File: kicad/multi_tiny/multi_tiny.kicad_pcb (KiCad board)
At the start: 2 copper layers, 105 x 91 mm, 59 parts, among them J1 Conn_02x03_Odd_Even, J2 28pin ZIF, J8 Conn_01x25, SW1 SW_SPDT, SW2 SW_SPDT, SW3 SW_SPDT, SW4 SW_SPST, U1 CD4052B, U2 CD4052B, U3 CD4052B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

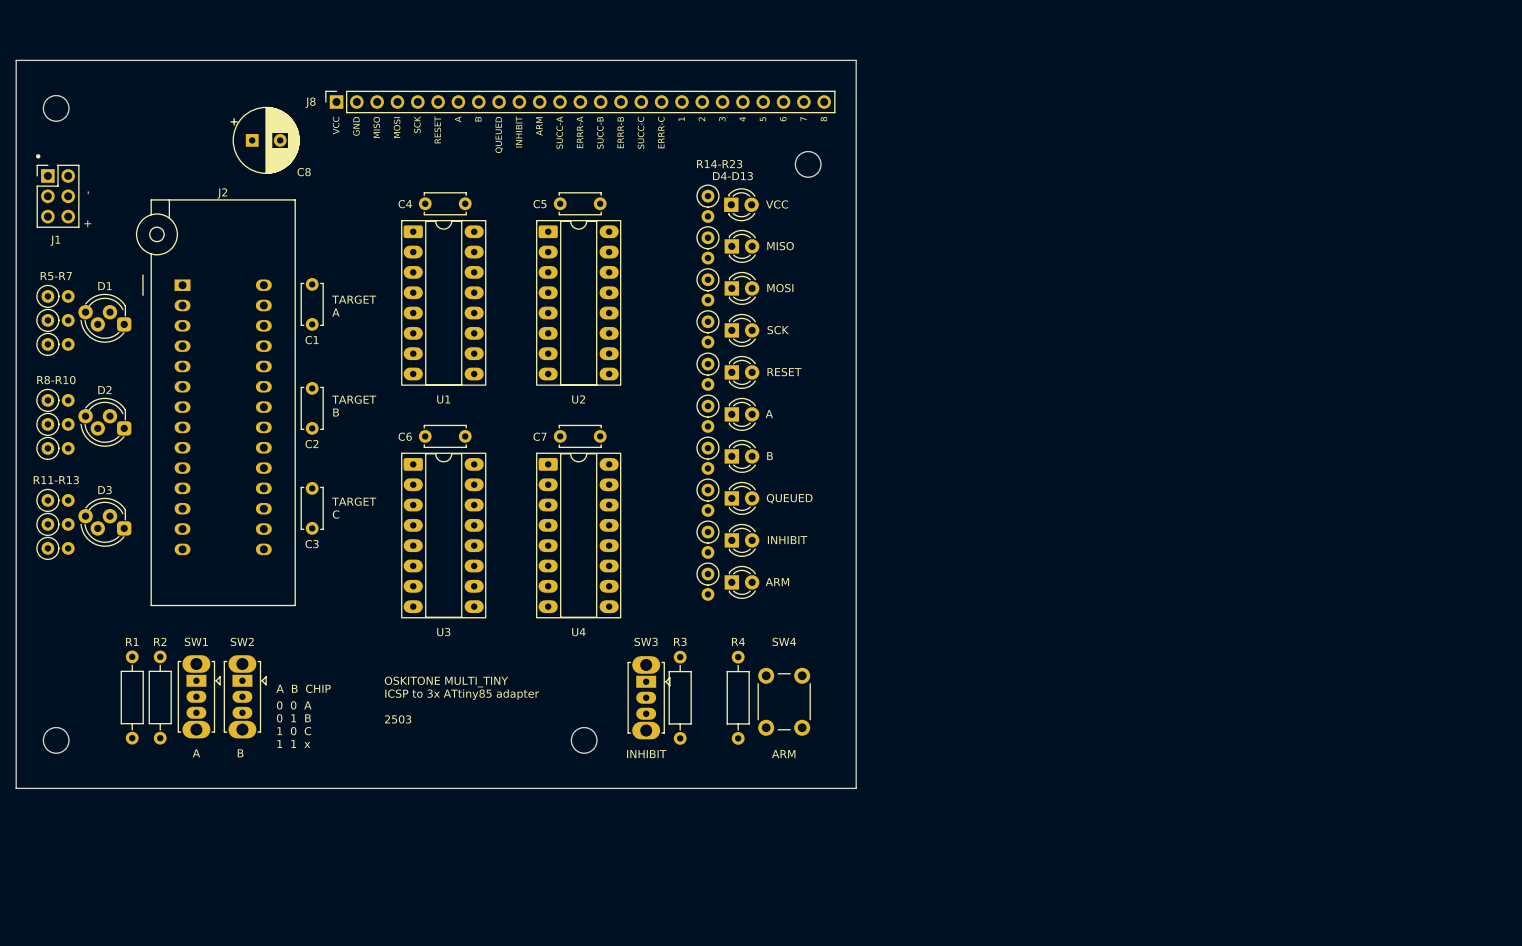
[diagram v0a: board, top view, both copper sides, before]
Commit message: Re-layout for flanked ZIF
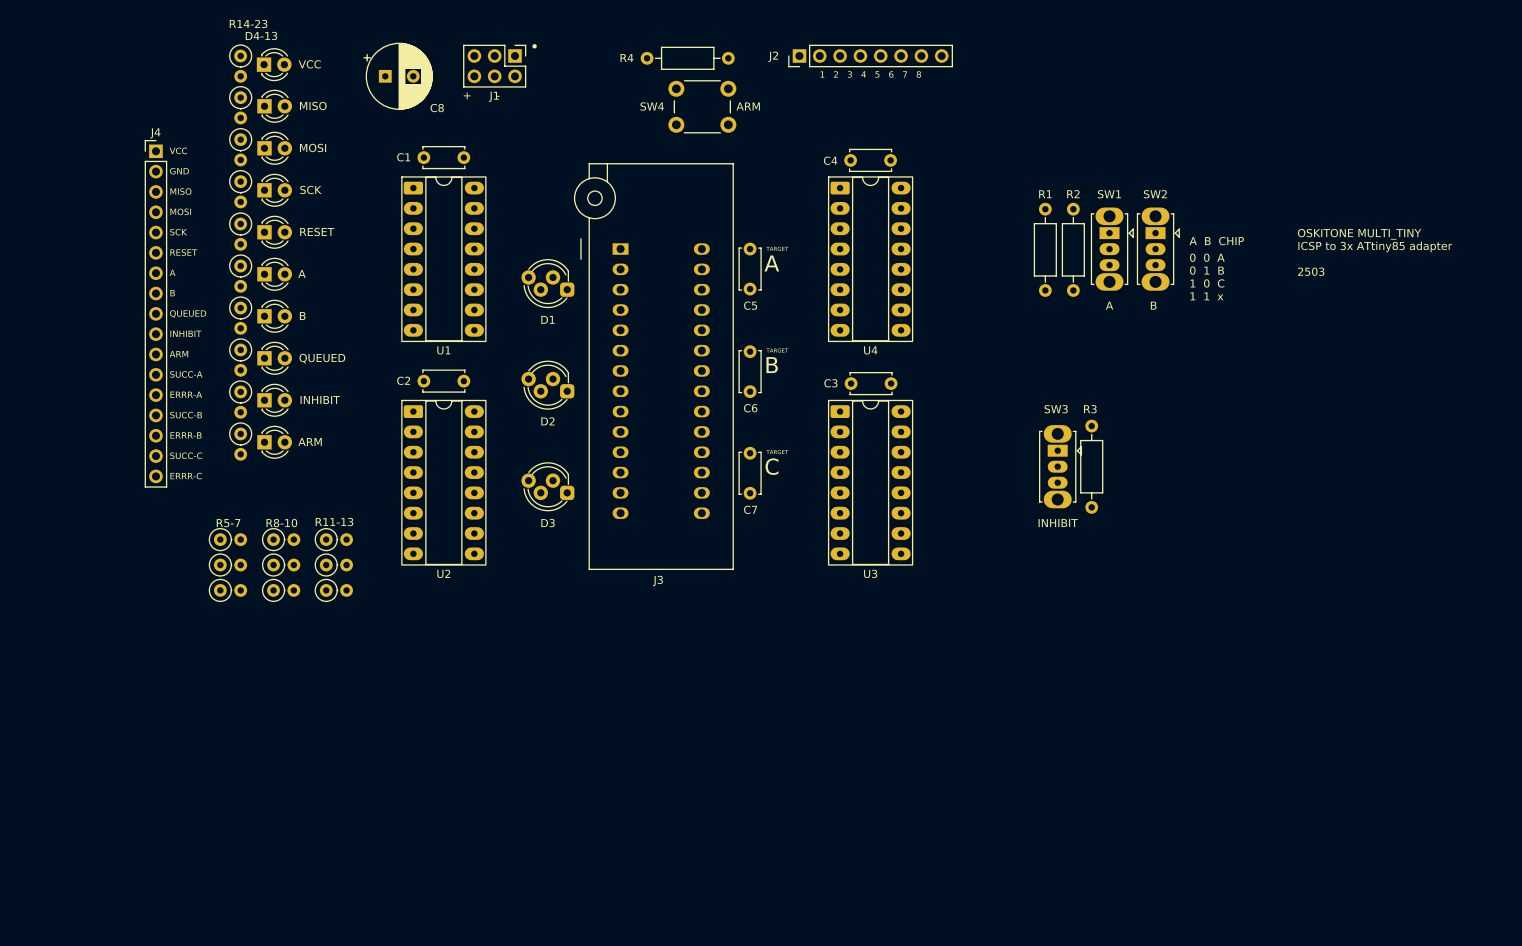
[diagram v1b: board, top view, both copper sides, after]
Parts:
- removed J8: Conn_01x25, Connector_PinSocket_2.54mm:PinSocket_1x25_P2.54mm_Vertical
- removed REF** (x4): MountingHole_3.2mm_M3, MountingHole:MountingHole_3.2mm_M3
- added J2: Conn_01x08, Connector_PinHeader_2.54mm:PinHeader_1x08_P2.54mm_Vertical, F.Cu at (168.9, 44.5)
- added J4: Conn_01x17, Connector_PinHeader_2.54mm:PinHeader_1x17_P2.54mm_Vertical, F.Cu at (88.5, 56.4)
- moved R1 127.1 mm to (199.6, 63.6)
- moved R2 127.1 mm to (203.1, 63.6)
- moved SW1 127.1 mm to (207.7, 66.6)
- moved SW2 127.1 mm to (213.4, 66.6)
- moved R4 75.7 mm to (149.9, 44.7), turned to 0 degrees
- moved SW4 75.0 mm to (153.5, 48.5), turned to 0 degrees
- moved C3 68.6 mm to (175.4, 85.4), turned to 0 degrees
- moved R14 61.0 mm to (99.1, 44.5)
- moved R15 61.0 mm to (99.1, 49.7)
- moved R16 61.0 mm to (99.1, 54.9)
- moved R17 61.0 mm to (99.1, 60.2)
- moved R18 61.0 mm to (99.1, 65.5)
- moved R19 61.0 mm to (99.1, 70.7)
- moved R20 61.0 mm to (99.1, 76.0)
- moved R21 61.0 mm to (99.1, 81.2)
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- renumbered J2 to J3
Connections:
- U3 pad 1: 4-A -> 3-A
- U3 pad 12: 3-A -> 4-A
- U3 pad 13: 3 -> 4
- U3 pad 14: 3-B -> 4-B
- U3 pad 15: 3-C -> 4-C
- U3 pad 2: 4-C -> 3-C
- U3 pad 3: 4 -> 3
- U3 pad 5: 4-B -> 3-B
- U4 pad 1: 8-A -> 7-A
- U4 pad 12: 7-A -> 8-A
- U4 pad 13: 7 -> 8
- U4 pad 14: 7-B -> 8-B
- U4 pad 15: 7-C -> 8-C
- U4 pad 2: 8-C -> 7-C
- U4 pad 3: 8 -> 7
- U4 pad 5: 8-B -> 7-B
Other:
- board outline removed
- board text added: "1 2 3 4 5 6 7 8"
- board text added: "C"
- board text added: "D4-13"
- board text added: "R11-13"
- board text added: "R14-23"
- board text added: "R5-7"
- board text added: "R8-10"
- board text added: "TARGET"
- board text added: "TODO: - test ZIF socket on print - mounting holes - rig holes on ZIF X rows - fix ICSP label? - header breadboard accessible"
- board text added: "VCC GND MISO MOSI SCK RESET A B QUEUED INHIBIT ARM SUCC-A ERRR-A SUCC-B ERRR-B SUCC-C ERRR-C"
- board text removed: "D4-D13"
- board text removed: "R11-R13"
- board text removed: "R14-R23"
- board text removed: "R5-R7"
- board text removed: "R8-R10"
- board text removed: "TARGET A"
- board text removed: "TARGET B"
- board text removed: "TARGET C"
- board text removed: "VCC GND MISO MOSI SCK RESET A B QUEUED INHIBIT ARM SUCC-A ERRR-A SUCC-B ERRR-B SUCC-C ERRR-C 1 2 3 4 5 6 7 8"

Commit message: Re-layout
* Fix ZIF dimensions
* IO refinements: ditch inhibit switch, pullups
  on external controls, add clear button
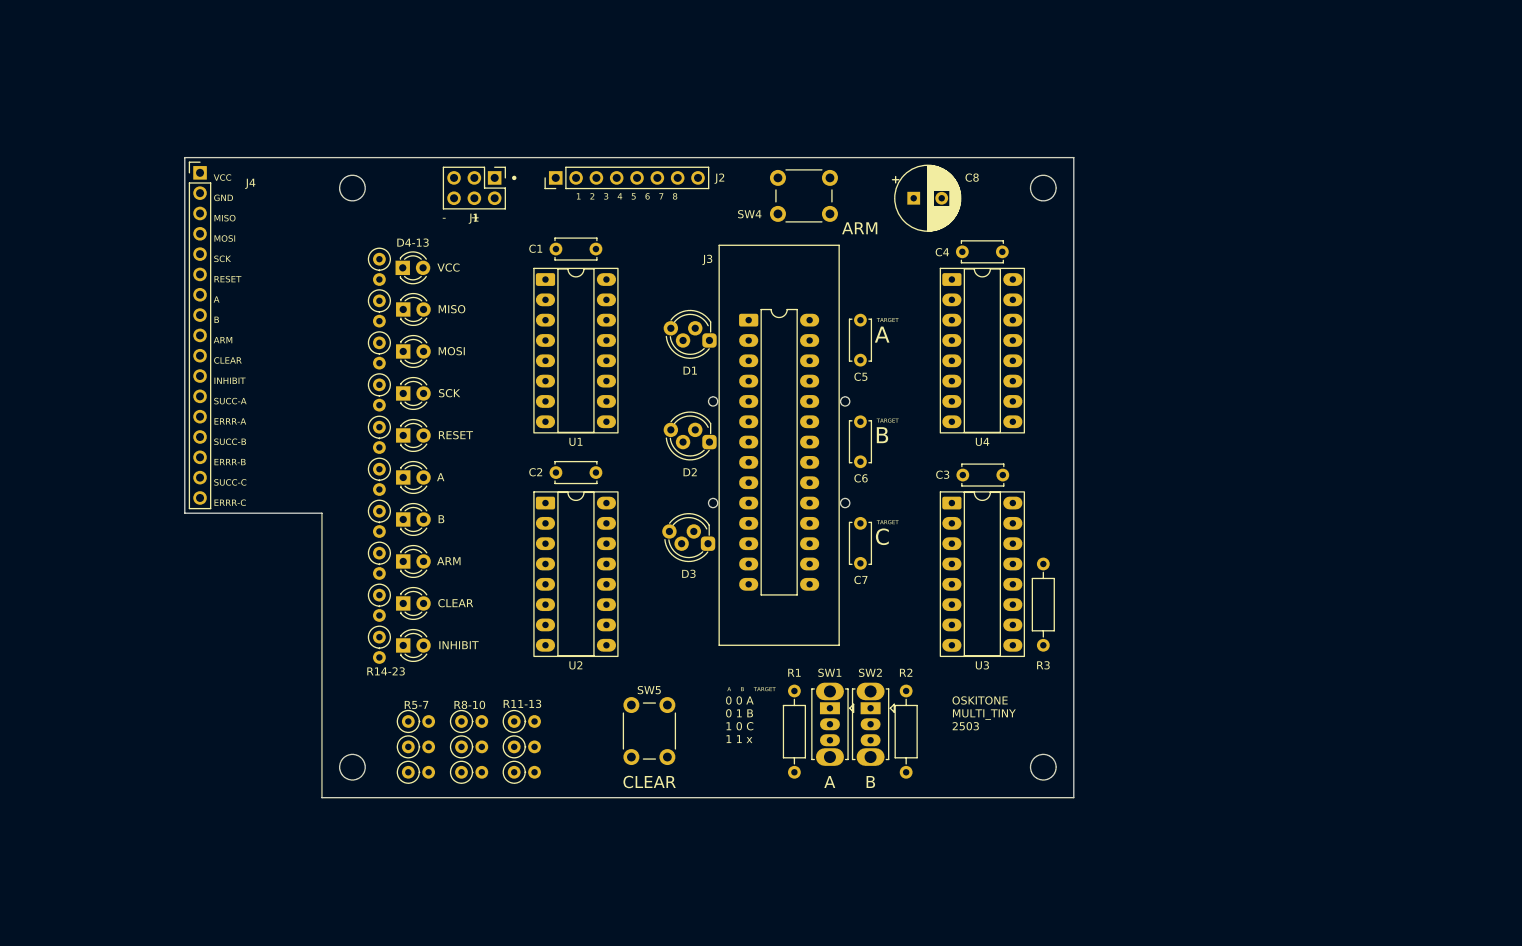
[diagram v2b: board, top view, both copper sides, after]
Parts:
- removed R4: 10k, Resistor_THT:R_Axial_DIN0207_L6.3mm_D2.5mm_P10.16mm_Horizontal
- removed SW3: SW_SPDT, Button_Switch_THT:SW_Slide_SPDT_Straight_CK_OS102011MS2Q
- added ?: , , F.Cu at (174.6, 100.3)
- added REF**: MountingHole_3.2mm_M3, MountingHole:MountingHole_3.2mm_M3, F.Cu at (113.0, 61.0)
- added REF**: ToolingHole_1.152mm, MountingHole:ToolingHole_1.152mm, F.Cu at (174.6, 87.6)
- added REF**: ToolingHole_1.152mm, MountingHole:ToolingHole_1.152mm, F.Cu at (158.1, 100.3)
- added REF**: MountingHole_3.2mm_M3, MountingHole:MountingHole_3.2mm_M3, F.Cu at (199.4, 61.0)
- added REF**: ToolingHole_1.152mm, MountingHole:ToolingHole_1.152mm, F.Cu at (158.1, 87.6)
- added REF**: MountingHole_3.2mm_M3, MountingHole:MountingHole_3.2mm_M3, F.Cu at (199.4, 133.3)
- added REF**: MountingHole_3.2mm_M3, MountingHole:MountingHole_3.2mm_M3, F.Cu at (113.0, 133.3)
- added SW5: SW_SPST, Button_Switch_THT:SW_PUSH_6mm, F.Cu at (147.9, 132.1)
- D11: value QUEUED -> ARM
- D12: value INHIBIT -> CLEAR
- D13: value ARM -> INHIBIT
- J3: footprint Socket:DIP_Socket-28_W6.9_W7.62_W10.16_W12.7_W13.5_3M_228-4817-00-0602J -> Package_DIP:DIP-28_W7.62mm_LongPads
- moved SW2 69.3 mm to (177.8, 126.0)
- moved SW1 68.9 mm to (172.7, 126.0)
- moved R1 67.9 mm to (168.3, 123.8)
- moved C8 67.8 mm to (183.2, 62.2)
- moved R2 63.7 mm to (182.2, 123.8)
- moved J2 34.1 mm to (138.4, 59.7)
- moved R13 32.7 mm to (133.3, 134.0)
- moved R7 32.7 mm to (120.0, 134.0)
- moved R10 32.7 mm to (126.7, 134.0)
- moved R11 32.7 mm to (133.3, 127.6)
- moved R12 32.7 mm to (133.3, 130.8)
- moved R5 32.7 mm to (120.0, 127.6)
- moved R6 32.7 mm to (120.0, 130.8)
- moved R8 32.7 mm to (126.7, 127.6)
- moved R9 32.7 mm to (126.7, 130.8)
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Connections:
- J4 pad 10: INHIBIT -> CLEAR
- J4 pad 11: ARM -> INHIBIT
- J4 pad 9: QUEUED -> ARM
- R21 pad 1: QUEUED -> ARM
- R22 pad 1: INHIBIT -> CLEAR
- R23 pad 1: ARM -> INHIBIT
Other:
- board outline added: 111.1 x 80 mm
- board text added: "- +"
- board text added: "CLEAR"
- board text added: "OSKITONE MULTI_TINY 2503"
- board text added: "TODO: - proper ZIF footprint - branding - print test: ZIF, X holes, breadboard - something in cutout?"
- board text added: "VCC GND MISO MOSI SCK RESET A B ARM CLEAR INHIBIT SUCC-A ERRR-A SUCC-B ERRR-B SUCC-C ERRR-C"
- board text removed: "+ -"
- board text removed: "A B CHIP"
- board text removed: "INHIBIT"
- board text removed: "OSKITONE MULTI_TINY ICSP to 3x ATtiny85 adapter 2503"
- board text removed: "TODO: - test ZIF socket on print - mounting holes - rig holes on ZIF X rows - fix ICSP label? - header breadboard accessible"
- board text removed: "VCC GND MISO MOSI SCK RESET A B QUEUED INHIBIT ARM SUCC-A ERRR-A SUCC-B ERRR-B SUCC-C ERRR-C"

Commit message: Square PCB
and put a lil breakaway ruler in the cutout
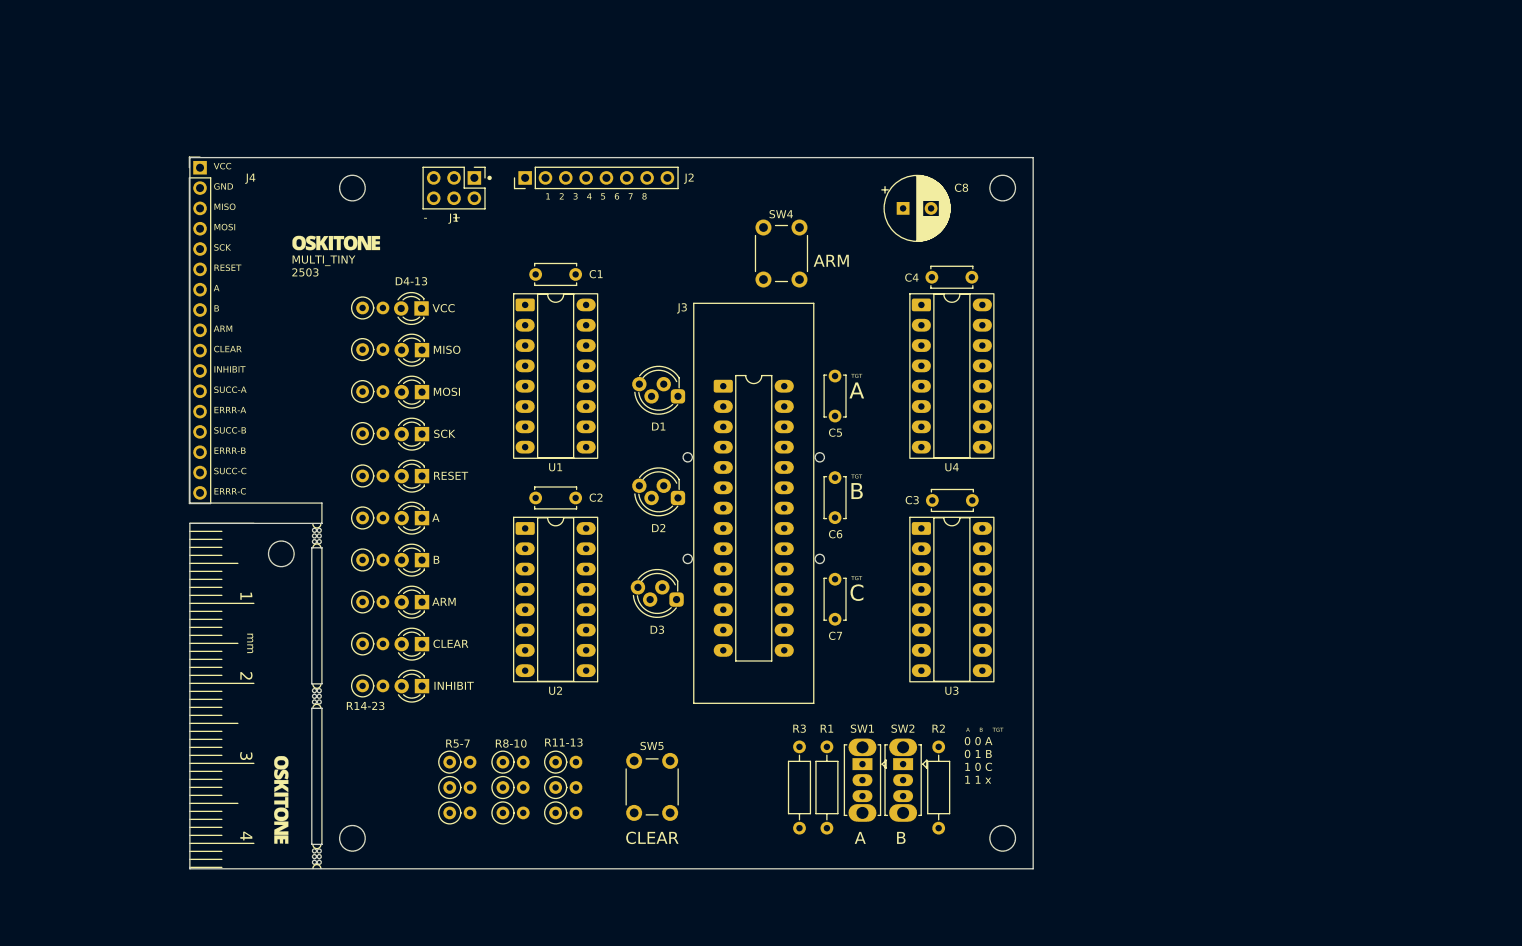
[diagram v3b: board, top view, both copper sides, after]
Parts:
- removed ?: , 
- added REF**: MountingHole_3.2mm_M3, MountingHole:MountingHole_3.2mm_M3, F.Cu at (104.1, 106.7)
- added REF**: ToolingHole_1.152mm, MountingHole:ToolingHole_1.152mm, F.Cu at (171.4, 107.3)
- added Ref**: Val**, parts_cafe:branding, F.Cu at (104.2, 137.4)
- added Ref**: Val**, parts_cafe:branding, F.Cu at (111.0, 67.8)
- added mouse-bite-1mm-3mm: VAL**, mouse-bite:mouse-bite-1mm-3mm, F.Cu at (108.6, 144.5)
- added mouse-bite-1mm-3mm: VAL**, mouse-bite:mouse-bite-1mm-3mm, F.Cu at (108.6, 124.5)
- added mouse-bite-1mm-3mm: VAL**, mouse-bite:mouse-bite-1mm-3mm, F.Cu at (108.6, 104.4)
- moved R3 44.9 mm to (168.9, 141.0), turned to 90 degrees
- moved SW4 11.7 mm to (164.4, 72.4), turned to 90 degrees
- moved REF** 10.2 mm to (194.3, 142.2)
- moved REF** 8.89 mm to (113.0, 142.2)
- moved J3 8.84 mm to (159.4, 85.7)
- moved R1 8.08 mm to (172.3, 130.8)
- moved R2 8.08 mm to (186.3, 130.8)
- moved SW1 8.08 mm to (176.8, 133.0)
- moved SW2 8.08 mm to (181.9, 133.0)
- moved D1 8.02 mm to (153.7, 87.0)
- moved D2 8.02 mm to (153.7, 99.7)
- moved D3 8.02 mm to (153.5, 112.4)
- moved C5 7.67 mm to (173.4, 89.5)
- moved C6 7.67 mm to (173.4, 102.2)
- moved C7 7.67 mm to (173.4, 114.9)
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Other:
- board size 111.1 x 80 mm -> 105.4 x 88.9 mm
- board text added: "1"
- board text added: "2"
- board text added: "3"
- board text added: "4"
- board text added: "MULTI_TINY 2503"
- board text added: "TGT"
- board text added: "TODO: - proper ZIF footprint"
- board text added: "in"
- board text added: "mm"
- board text removed: "TARGET"
- board text removed: "TODO: - proper ZIF footprint - branding - print test: ZIF, X holes, breadboard - something in cutout?"
